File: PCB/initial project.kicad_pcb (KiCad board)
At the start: 2 copper layers, 81 x 62.5 mm, 21 parts, among them SW1 SW_Push, SW2 SW_Push, SW3 SW_Push, SW4 SW_Push, SW5 SW_Push, SW6 SW_Push, U1 MOUDLE-SEEEDUINO-XIAO, U2 ER_OLEDM0.91_1x-I2C

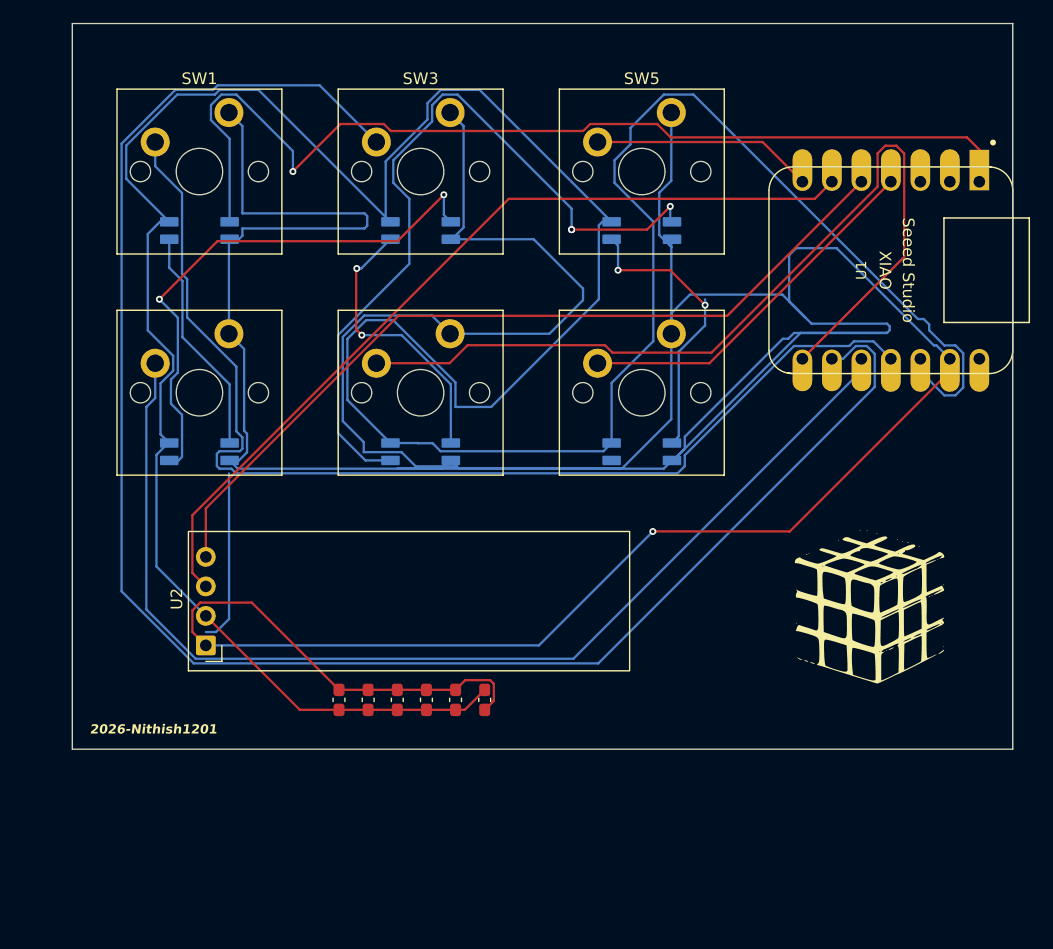
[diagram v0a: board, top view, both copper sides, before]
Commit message: Correction of LED power rail
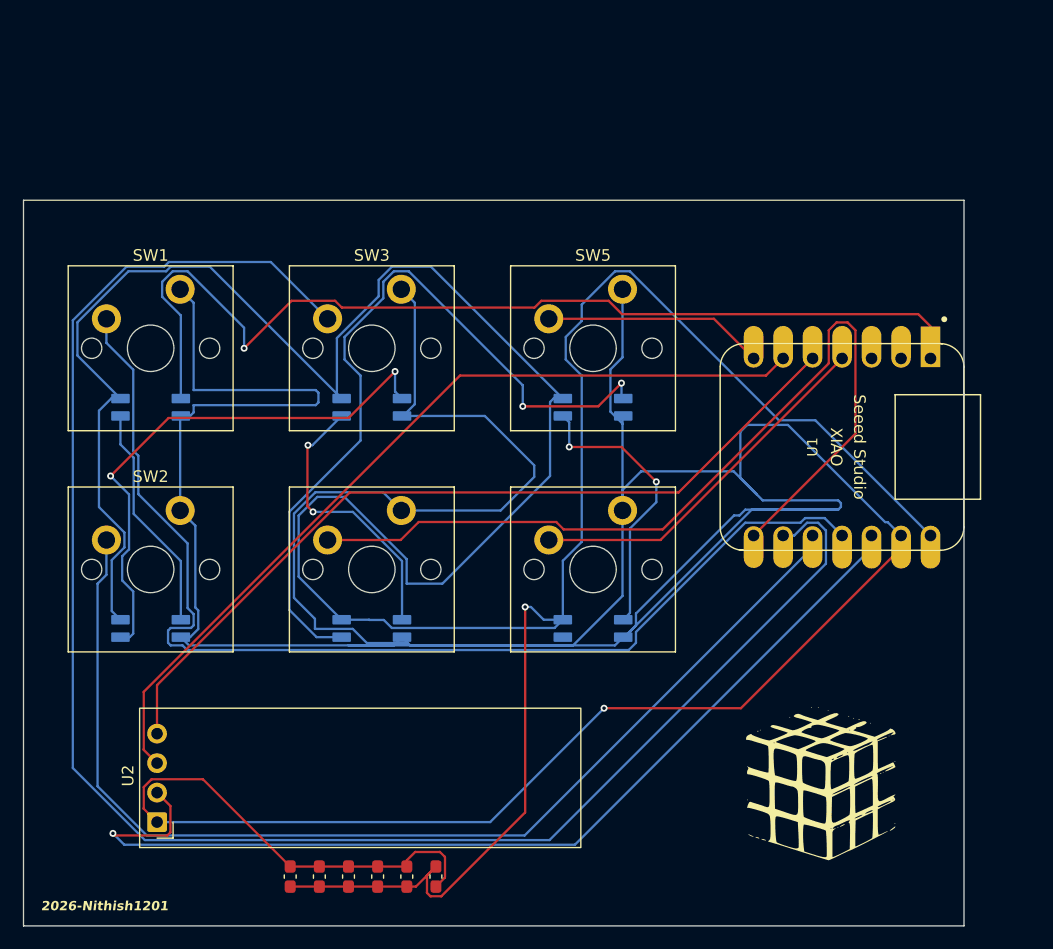
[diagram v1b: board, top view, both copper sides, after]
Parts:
- SW2: footprint PCM_Switch_Keyboard_Cherry_MX:SW_Cherry_MX_PCB_1.00u -> PCM_Switch_Keyboard_Cherry_MX:SW_Cherry_MX_PCB
- moved C2 15.8 mm to (183.3, 143.2)
- moved C3 15.8 mm to (185.8, 143.2)
- moved C4 15.8 mm to (188.3, 143.2)
- moved C5 15.8 mm to (190.8, 143.2)
- moved C6 15.8 mm to (193.3, 143.2)
- moved C7 15.8 mm to (195.8, 143.2)
- moved D1 15.8 mm to (171.2, 97.7)
- moved D2 15.8 mm to (171.2, 116.8)
- moved D3 15.8 mm to (190.3, 97.7)
- moved D4 15.8 mm to (190.3, 116.8)
- moved D5 15.8 mm to (209.3, 97.7)
- moved D6 15.8 mm to (209.3, 116.8)
- moved G*** 15.8 mm to (229.3, 135.2)
- moved SW1 15.8 mm to (171.2, 97.7)
- moved SW2 15.8 mm to (171.2, 116.8)
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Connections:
- C2 pad 1: +3V3 -> +5V
- C3 pad 1: +3V3 -> +5V
- C4 pad 1: +3V3 -> +5V
- C5 pad 1: +3V3 -> +5V
- C6 pad 1: +3V3 -> +5V
- C7 pad 2: +3V3 -> +5V
- D1 pad 1: +3V3 -> +5V
- D2 pad 1: +3V3 -> +5V
- D3 pad 1: +3V3 -> +5V
- D4 pad 1: +3V3 -> +5V
- D5 pad 1: +3V3 -> +5V
- D6 pad 1: +3V3 -> +5V
- U1 pad 14: unconnected-(U1-5V-Pad14) -> +5V
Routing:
- net +5V: track 0.00 -> 278.7 mm, vias 0 -> 1
- net +3V3: track 284.7 -> 86.4 mm, vias 0 -> 1
- net (no net): track 15.0 -> 0.00 mm
- net GND: track 420.0 -> 420.8 mm
- net Net-(D5-DOUT): track 25.2 -> 24.7 mm
- net Net-(D4-DOUT): vias 3 -> 2

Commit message: Fixed orientation of LEDs
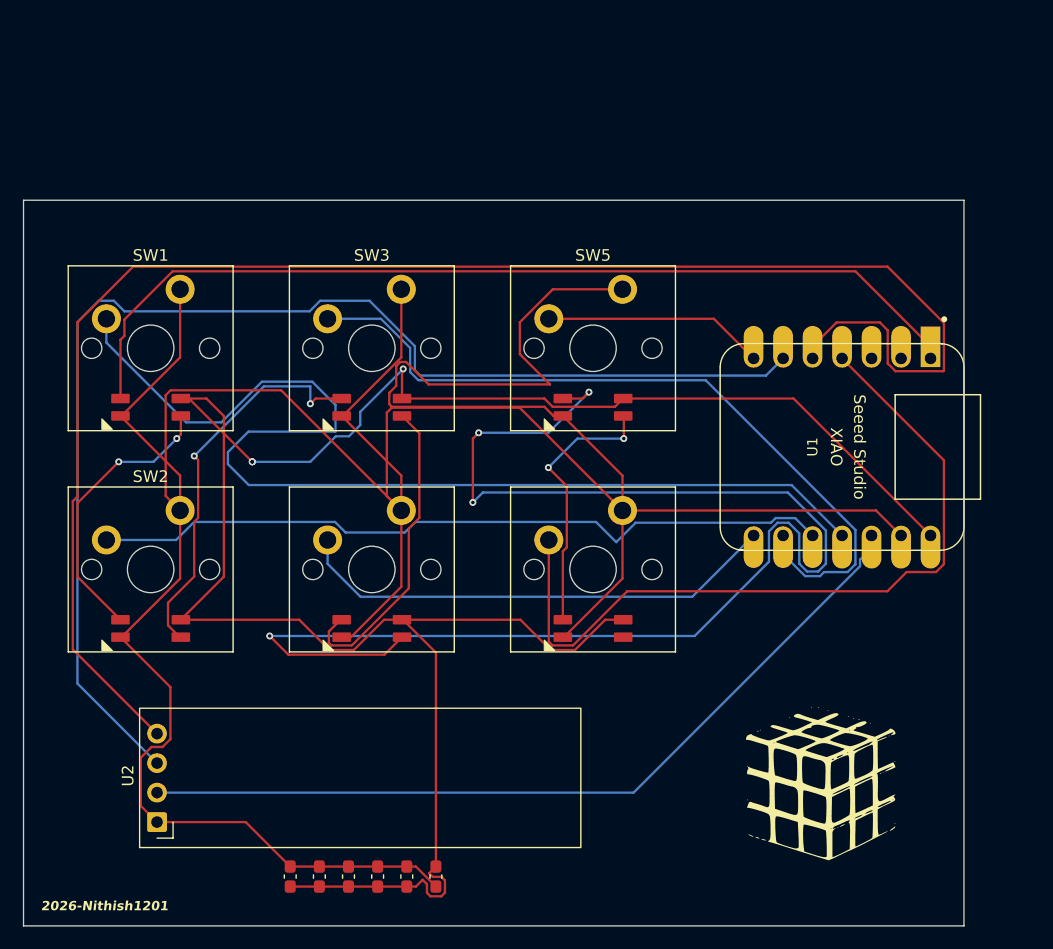
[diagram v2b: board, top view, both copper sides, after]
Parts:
- D1, D2, D3, D4, D5, D6: moved to B.Cu
- turned D1 to 180 degrees
- turned D2 to 180 degrees
- turned D3 to 180 degrees
- turned D4 to 180 degrees
- turned D5 to 180 degrees
- turned D6 to 180 degrees
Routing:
- net GND: track 420.8 -> 285.6 mm, vias 1 -> 0
- net +5V: track 278.7 -> 185.5 mm, vias 1 -> 3
- net Net-(U1-PA7_A8_D8_SCK): track 149.2 -> 66.2 mm
- net Net-(U1-PA8_A4_D4_SDA): track 72.3 -> 138.0 mm
- net Net-(D4-DOUT): track 67.2 -> 124.3 mm, vias 2 -> 4
- net Net-(U1-PA11_A3_D3): track 31.7 -> 67.2 mm
- net Net-(U1-PB09_A7_D7_RX): track 77.0 -> 42.1 mm
- net Net-(U1-PA9_A5_D5_SCL): track 73.6 -> 107.6 mm
- net Net-(U1-PA5_A9_D9_MISO): track 96.2 -> 64.4 mm
- net +3V3: track 86.4 -> 71.7 mm, vias 1 -> 0
- net Net-(D2-DOUT): track 46.9 -> 34.2 mm
- net Net-(D1-DIN): track 86.9 -> 81.8 mm, vias 1 -> 0
- net Net-(D1-DOUT): track 19.7 -> 24.5 mm, vias 0 -> 2
- net Net-(D3-DOUT): track 24.4 -> 27.4 mm, vias 2 -> 0
- net Net-(U1-PA6_A10_D10_MOSI): track 97.1 -> 95.7 mm
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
